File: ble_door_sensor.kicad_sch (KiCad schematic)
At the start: 29 parts, among them IC1 MLPF-NRG-01D3, IC2 TCS40DPR,LF, U1 STM32WB09KEVx, Y1 NX2016SA-32M-EXS00A-CS06465, Y2 32.768KHz

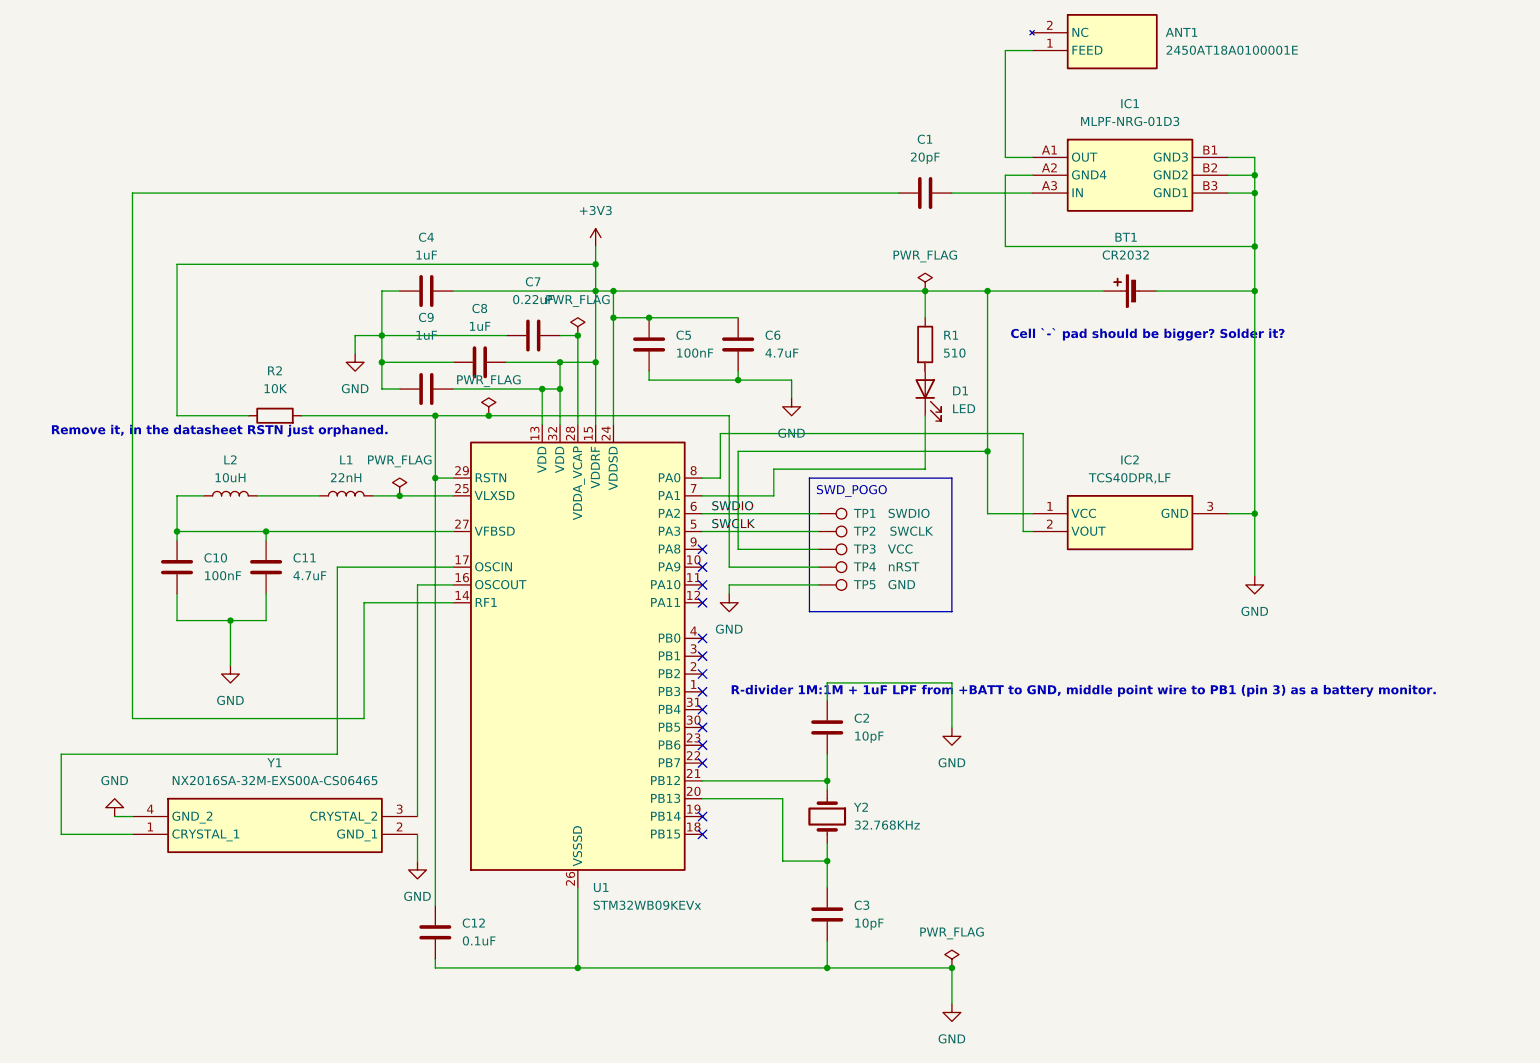
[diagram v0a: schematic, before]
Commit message: Rev B: VDDA_VCAP cap + battery divider + JST-MX 4P connector
PCB Rev B (title block "1.1/B", comment "Added: GPIOs connector.").
Boards ordered from fab. Folds in everything that was hand-reworked
on Rev A plus a new expansion connector for future modularity work.

Schematic + PCB changes vs Rev A:

1. **VDDA_VCAP decoupling cap** (0.22 µF) on STM32WB09KEVx pin 28.
   Rev A was missing this — caused HCI Hardware_Code 0x01 on every
   advert TX until hand-soldered. Now built into the layout.

2. **External battery-monitor divider**: R1 = 1 MΩ from cell+ →
   midpoint, R2 = 1 MΩ midpoint → GND, C1 = 1 µF X7R as a reservoir
   cap on the R2 side (NOT in series). Midpoint routed to PB1 =
   ADC1_VINP1. Quiescent ~1.5 µA. Replaces the Rev A hand-solder.

   Two bring-up gotchas were discovered with this circuit and are
   documented in the firmware repo:
     - PB3 (the original choice per all WB09 NUCLEO ADC examples)
       has a legacy JTDO default ~40 kΩ pull-up that can't be cleared
       from software. PB1 = VINP1 is the working alternative.
     - The WB0 ADC's sample-and-hold pulls ~7 nC per conversion;
       10 nF reservoir cap is too small (causes ~700 mV droop).
       1 µF X7R is the working value.

3. **JST-MX 4P expansion connector** on PA8 / PA9 / PA10 / PA11.
   Adds 4 GPIO lines to an external connector for future modular
   expansion (planned: motherboard + sensor-extension architecture
   where this connector is the m/b-side socket).

README:
- Replaces hero-image placeholder with side-A + side-B KiCad
  renders embedded via raw.githubusercontent URLs from sensorkit.

Tagged pcb-rev-b on this commit; pcb-rev-a remains as the
"as-fabricated original" reference.

Co-Authored-By: Claude Opus 4.7 (1M context) <noreply@anthropic.com>
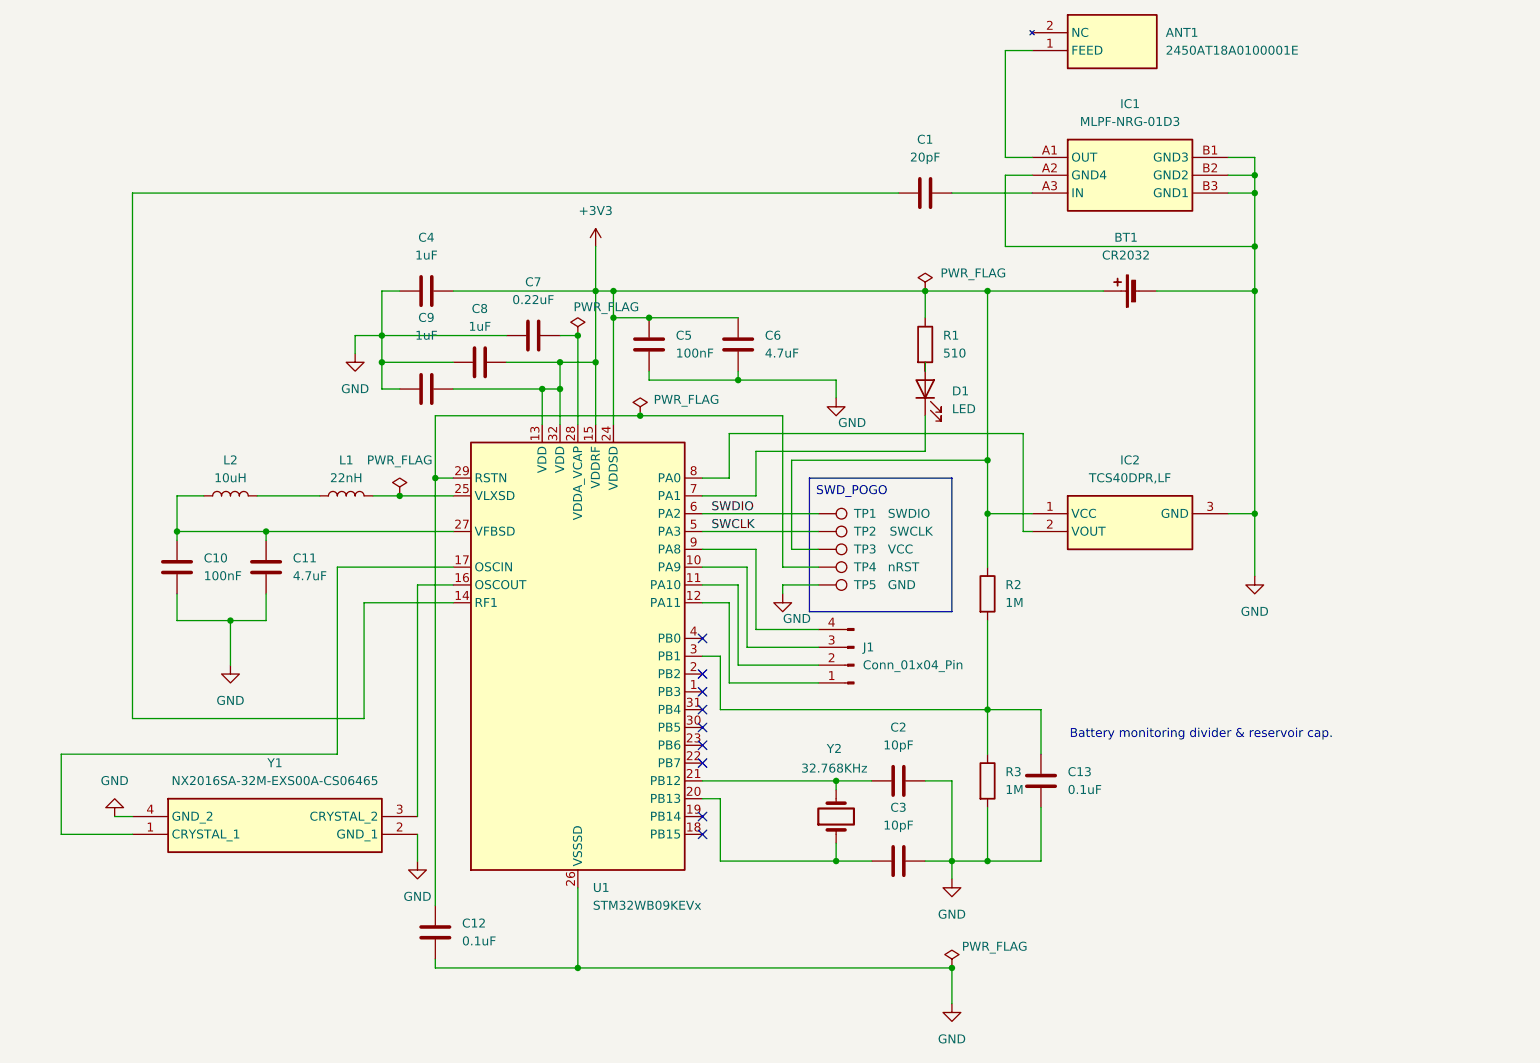
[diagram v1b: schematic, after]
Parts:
- added C13: 0.1uF, Capacitor_SMD:C_0603_1608Metric, symbol Device:C
- added J1: Conn_01x04_Pin, KiCad:JST_MX_4P-1_25, symbol Connector:Conn_01x04_Pin
- added R3: 1M, Resistor_SMD:R_0402_1005Metric, symbol Device:R
- R2: value 10K -> 1M
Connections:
- net GND: now also C2.2, C13.2, R3.2; no longer C2.1
- net at U1.10 (PA9): now also J1.3 (Pin_3)
- net at U1.11 (PA10): now also J1.2 (Pin_2)
- net at U1.12 (PA11): now also J1.1 (Pin_1)
- net at C3.1, U1.20 (PB13): now also Y2.1; no longer Y2.2
- net at C12.1, TP4.1, U1.29 (RSTN): no longer R2.2
- net at U1.3 (PB1): now also R2.2, C13.1, R3.1
- net at U1.9 (PA8): now also J1.4 (Pin_4)
- new net: C2.1, U1.21 (PB12), Y2.2
- no-connect marks 14 -> 9
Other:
- note added: "Battery monitoring divider & reservoir cap."
- note removed: "Cell `-` pad should be bigger? Solder it?"
- note removed: "R-divider 1M:1M + 1uF LPF from +BATT to GND, middle point wire to PB1 (pin 3) as a battery monitor."
- note removed: "Remove it, in the datasheet RSTN just orphaned."
- company: (none) -> SpectralWarrior
- moved on the sheet: C2, C3, Y2
